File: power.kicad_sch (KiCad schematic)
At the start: 160 parts, among them Q10 SI7613DN-T1-GE3, Q14 BC817-25W, Q15 BC817-25W, Q2 BC817-25W, Q3 DZDH0401DW, Q4 DZDH0401DW, Q5 SI7613DN-T1-GE3, Q6 SI7613DN-T1-GE3, Q7 BC817-25W, Q8 BC817-25W, Q9 SI7613DN-T1-GE3, U1 LT8350RV#PBF, U10 LM3881MME_NOPB, U2 MP2386GG, U3 TPS65983BAZBHR, U9 LM1117MP-3.3_NOPB

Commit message: Run kmake loclib
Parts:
- C10, C13, C15, C17, C8: footprint antmicro-footprints:C_1206_3216Metric -> thunderbolt-adapter-footprints:C_1206_3216Metric; symbol antmicroCapacitorsmisc:C_22u_1206_35V -> thunderbolt-adapter:C_22u_1206_35V
- C11, C12, C127, C128, C7, C9: footprint antmicro-footprints:C_0805_2012Metric -> thunderbolt-adapter-footprints:C_0805_2012Metric; symbol antmicroCapacitorsmisc:C_10u_0805_35V -> thunderbolt-adapter:C_10u_0805_35V
- C119, C122, C38, C40, C43, C46, C50: footprint antmicro-footprints:C_0603_1608Metric -> thunderbolt-adapter-footprints:C_0603_1608Metric; symbol antmicroCapacitors0603:C_22u_16V_0603 -> thunderbolt-adapter:C_22u_16V_0603
- C129, C14, C24, C26, C28, C29, C32: footprint antmicro-footprints:C_0402_1005Metric -> thunderbolt-adapter-footprints:C_0402_1005Metric; symbol antmicroCapacitors0402:C_100n_0402 -> thunderbolt-adapter:C_100n_0402
- C130: footprint antmicro-footprints:C_0402_1005Metric -> thunderbolt-adapter-footprints:C_0402_1005Metric; symbol antmicroCapacitors0402:C_10n_0402 -> thunderbolt-adapter:C_10n_0402
- C16, C27, C31: footprint antmicro-footprints:C_0402_1005Metric -> thunderbolt-adapter-footprints:C_0402_1005Metric; symbol antmicroCapacitors0402:C_220n_0402 -> thunderbolt-adapter:C_220n_0402
- C18, C22, C25, C34: footprint antmicro-footprints:C_0402_1005Metric -> thunderbolt-adapter-footprints:C_0402_1005Metric; symbol antmicroCapacitors0402:C_1u_0402 -> thunderbolt-adapter:C_1u_0402
- C19: footprint antmicro-footprints:C_0402_1005Metric -> thunderbolt-adapter-footprints:C_0402_1005Metric; symbol antmicroCapacitors0402:C_22n_0402 -> thunderbolt-adapter:C_22n_0402
- C20, C21: footprint antmicro-footprints:C_0402_1005Metric -> thunderbolt-adapter-footprints:C_0402_1005Metric; symbol antmicroCapacitors0402:C_4u7_25V_0402 -> thunderbolt-adapter:C_4u7_25V_0402
- C23, C39: footprint antmicro-footprints:C_0402_1005Metric -> thunderbolt-adapter-footprints:C_0402_1005Metric; symbol antmicroCapacitors0402:C_10u_0402 -> thunderbolt-adapter:C_10u_0402
- C30: footprint antmicro-footprints:C_0402_1005Metric -> thunderbolt-adapter-footprints:C_0402_1005Metric; symbol antmicroCapacitors0402:C_4n7_0402 -> thunderbolt-adapter:C_4n7_0402
- C33: footprint antmicro-footprints:C_0402_1005Metric -> thunderbolt-adapter-footprints:C_0402_1005Metric; symbol antmicroCapacitors0402:C_33p_0402 -> thunderbolt-adapter:C_33p_0402
- C35, C36, C37: footprint antmicro-footprints:C_0402_1005Metric -> thunderbolt-adapter-footprints:C_0402_1005Metric; symbol antmicroCapacitors0402:C_2u2_0402 -> thunderbolt-adapter:C_2u2_0402
- C41, C44, C47: footprint antmicro-footprints:C_0603_1608Metric -> thunderbolt-adapter-footprints:C_0603_1608Metric; symbol antmicroCapacitors0603:C_22u_0603 -> thunderbolt-adapter:C_22u_0603
- C42, C48: footprint antmicro-footprints:C_0805_2012Metric -> thunderbolt-adapter-footprints:C_0805_2012Metric; symbol antmicroCapacitorsmisc:C_22u_25V_0805 -> thunderbolt-adapter:C_22u_25V_0805
- C45, C49: footprint antmicro-footprints:C_0402_1005Metric -> thunderbolt-adapter-footprints:C_0402_1005Metric; symbol antmicroCapacitors0402:C_220p_0402 -> thunderbolt-adapter:C_220p_0402
- D1: footprint antmicro-footprints:D_SOD-323F -> thunderbolt-adapter-footprints:D_SOD-323F; symbol antmicroDiodesZenerSingle:MM3Z3V3C -> thunderbolt-adapter:MM3Z3V3C
- D2, D3, D5: footprint antmicro-footprints:LED_0603_1608Metric_G -> thunderbolt-adapter-footprints:LED_0603_1608Metric_G; symbol antmicroLEDIndicationDiscrete:LED_G_0603_KP-1608CGCK -> thunderbolt-adapter:LED_G_0603_KP-1608CGCK
- FB1, FB2, FB3, FB5, FB6: footprint antmicro-footprints:FB_0805_2012Metric -> thunderbolt-adapter-footprints:FB_0805_2012Metric; symbol antmicroFerriteBeadsandChips:BLM21SN300SZ1D -> thunderbolt-adapter:BLM21SN300SZ1D
- L1: footprint antmicro-footprints:L_Coilcraft-XAL7070 -> thunderbolt-adapter-footprints:L_Coilcraft-XAL7070; symbol antmicroFixedInductors:L_6u8_12.8A_Coilcraft-XAL7070 -> thunderbolt-adapter:L_6u8_12.8A_Coilcraft-XAL7070
- L2: footprint antmicro-footprints:L_Coilcraft-XAL5030 -> thunderbolt-adapter-footprints:L_Coilcraft-XAL5030; symbol antmicroFixedInductors:L_2u2_9.7A_Coilcraft-XAL5030 -> thunderbolt-adapter:L_2u2_9.7A_Coilcraft-XAL5030
- Q10, Q5, Q6, Q9: footprint antmicro-footprints:Vishay_PowerPAK_1212-8_Single -> thunderbolt-adapter-footprints:Vishay_PowerPAK_1212-8_Single; symbol antmicroTransistorsFETsMOSFETsSingle:SI7613DN-T1-GE3 -> thunderbolt-adapter:SI7613DN-T1-GE3
- Q14, Q15, Q2, Q7, Q8: footprint antmicro-footprints:SOT-323 -> thunderbolt-adapter-footprints:SOT-323; symbol antmicroTransistorsBipolarSingle:BC817-25W -> thunderbolt-adapter:BC817-25W
- Q3, Q4: footprint antmicro-footprints:SOT-363 -> thunderbolt-adapter-footprints:SOT-363; symbol antmicroPMICORControllersIdealDiodes:DZDH0401DW -> thunderbolt-adapter:DZDH0401DW
- R10, R121, R122, R124, R125, R135, R137, R139, R140, R141, R22, R23, R24, R29, R30, R33, R34, R4, R9, R92, R95, R96: footprint antmicro-footprints:R_0402_1005Metric -> thunderbolt-adapter-footprints:R_0402_1005Metric; symbol antmicroResistors0402:R_100k_0402 -> thunderbolt-adapter:R_100k_0402
- R11, R16, R17, R19, R2, R20, R32, R39, R44, R6, R8, R91, R93, R94: footprint antmicro-footprints:R_0402_1005Metric -> thunderbolt-adapter-footprints:R_0402_1005Metric; symbol antmicroResistors0402:R_10k_0402 -> thunderbolt-adapter:R_10k_0402
- R116, R120, R134, R136, R142, R143, R144: footprint antmicro-footprints:R_0402_1005Metric -> thunderbolt-adapter-footprints:R_0402_1005Metric; symbol antmicroResistors0402:R_1k_0402 -> thunderbolt-adapter:R_1k_0402
- R12, R123, R13, R138, R18, R26, R27, R31: footprint antmicro-footprints:R_0402_1005Metric -> thunderbolt-adapter-footprints:R_0402_1005Metric; symbol antmicroResistors0402:R_0R_0402 -> thunderbolt-adapter:R_0R_0402
- R14, R15: footprint antmicro-footprints:R_0402_1005Metric -> thunderbolt-adapter-footprints:R_0402_1005Metric; symbol antmicroResistors0402:R_3k3_0402 -> thunderbolt-adapter:R_3k3_0402
- R21: footprint antmicro-footprints:R_0402_1005Metric -> thunderbolt-adapter-footprints:R_0402_1005Metric; symbol antmicroResistors0402:R_1M_0402 -> thunderbolt-adapter:R_1M_0402
- R25: footprint antmicro-footprints:R_0402_1005Metric -> thunderbolt-adapter-footprints:R_0402_1005Metric; symbol antmicroResistors0402:R_12k_0402 -> thunderbolt-adapter:R_12k_0402
- R28: footprint antmicro-footprints:R_0402_1005Metric -> thunderbolt-adapter-footprints:R_0402_1005Metric; symbol antmicroResistors0402:R_124k_0402 -> thunderbolt-adapter:R_124k_0402
- R3, R46, R5, R97: footprint antmicro-footprints:R_0402_1005Metric -> thunderbolt-adapter-footprints:R_0402_1005Metric; symbol antmicroResistors0402:R_2k2_0402 -> thunderbolt-adapter:R_2k2_0402
- R35: footprint antmicro-footprints:R_0402_1005Metric -> thunderbolt-adapter-footprints:R_0402_1005Metric; symbol antmicroResistors0402:R_15k_0.1%_0402 -> thunderbolt-adapter:R_15k_0.1%_0402
- R36: footprint antmicro-footprints:R_0402_1005Metric -> thunderbolt-adapter-footprints:R_0402_1005Metric; symbol antmicroResistors0402:R_40k2_0402 -> thunderbolt-adapter:R_40k2_0402
- R37: footprint antmicro-footprints:R_0402_1005Metric -> thunderbolt-adapter-footprints:R_0402_1005Metric; symbol antmicroResistors0402:R_8k87_0402 -> thunderbolt-adapter:R_8k87_0402
- R38, R40: footprint antmicro-footprints:R_0402_1005Metric -> thunderbolt-adapter-footprints:R_0402_1005Metric; symbol antmicroResistors0402:R_5k1_0402 -> thunderbolt-adapter:R_5k1_0402
- R41: footprint antmicro-footprints:R_0603_1608Metric -> thunderbolt-adapter-footprints:R_0603_1608Metric; symbol antmicroResistors0603:R_0R_0603 -> thunderbolt-adapter:R_0R_0603
- R42: footprint antmicro-footprints:R_0402_1005Metric -> thunderbolt-adapter-footprints:R_0402_1005Metric; symbol antmicroResistors0402:R_330R_0402 -> thunderbolt-adapter:R_330R_0402
- R43: footprint antmicro-footprints:R_0402_1005Metric -> thunderbolt-adapter-footprints:R_0402_1005Metric; symbol antmicroResistors0402:R_110k_0402 -> thunderbolt-adapter:R_110k_0402
- R45: footprint antmicro-footprints:R_1206_3216Metric -> thunderbolt-adapter-footprints:R_1206_3216Metric; symbol antmicroResistorsmisc:R_0R02_1206 -> thunderbolt-adapter:R_0R02_1206
- R7: footprint antmicro-footprints:R_0402_1005Metric -> thunderbolt-adapter-footprints:R_0402_1005Metric; symbol antmicroResistors0402:R_24k_0402 -> thunderbolt-adapter:R_24k_0402
- R98, R99: footprint antmicro-footprints:R_0603_1608Metric -> thunderbolt-adapter-footprints:R_0603_1608Metric; symbol antmicroResistors0603:R_0R_22.4A_0603 -> thunderbolt-adapter:R_0R_22.4A_0603
- TP1, TP12, TP2, TP3, TP5, TP7, TP8: footprint antmicro-footprints:Testpoint_smd_1mm -> thunderbolt-adapter-footprints:Testpoint_smd_1mm; symbol antmicroTestPoints:TP_1mm_SMD -> thunderbolt-adapter:TP_1mm_SMD
- TP10, TP11: footprint antmicro-footprints:NetTie-2_SMD_Pad0.127mm -> thunderbolt-adapter-footprints:NetTie-2_SMD_Pad0.127mm; symbol antmicroShuntsJumpers:Net-Tie_2 -> thunderbolt-adapter:Net-Tie_2
- TP4, TP6: footprint antmicro-footprints:TP_SMD_0.75mm -> thunderbolt-adapter-footprints:TP_SMD_0.75mm; symbol antmicroTestPoints:TP_0.75mm_SMD -> thunderbolt-adapter:TP_0.75mm_SMD
- U1: footprint antmicro-footprints:QFN-32-4EP_4x6mm_P0.5mm -> thunderbolt-adapter-footprints:QFN-32-4EP_4x6mm_P0.5mm; symbol antmicroDCDCConverters:LT8350RV#PBF -> thunderbolt-adapter:LT8350RV#PBF
- U10: footprint antmicro-footprints:VSSOP-8_3x3mm_P0.65mm -> thunderbolt-adapter-footprints:VSSOP-8_3x3mm_P0.65mm; symbol antmicroPMICPowerSequencers:LM3881MME_NOPB -> thunderbolt-adapter:LM3881MME_NOPB
- U2: footprint antmicro-footprints:QFN-11_2x2mm_P0.5mm -> thunderbolt-adapter-footprints:QFN-11_2x2mm_P0.5mm; symbol antmicroDCDCConverters:MP2386GG -> thunderbolt-adapter:MP2386GG
- U3: footprint antmicro-footprints:IC_TPS65983BAZBHR -> thunderbolt-adapter-footprints:IC_TPS65983BAZBHR; symbol antmicroInterfaceControllers:TPS65983BAZBHR -> thunderbolt-adapter:TPS65983BAZBHR
- U9: footprint antmicro-footprints:SOT-223 -> thunderbolt-adapter-footprints:SOT-223; symbol antmicroPMICVoltageRegulatorsLinear:LM1117MP-3.3_NOPB -> thunderbolt-adapter:LM1117MP-3.3_NOPB

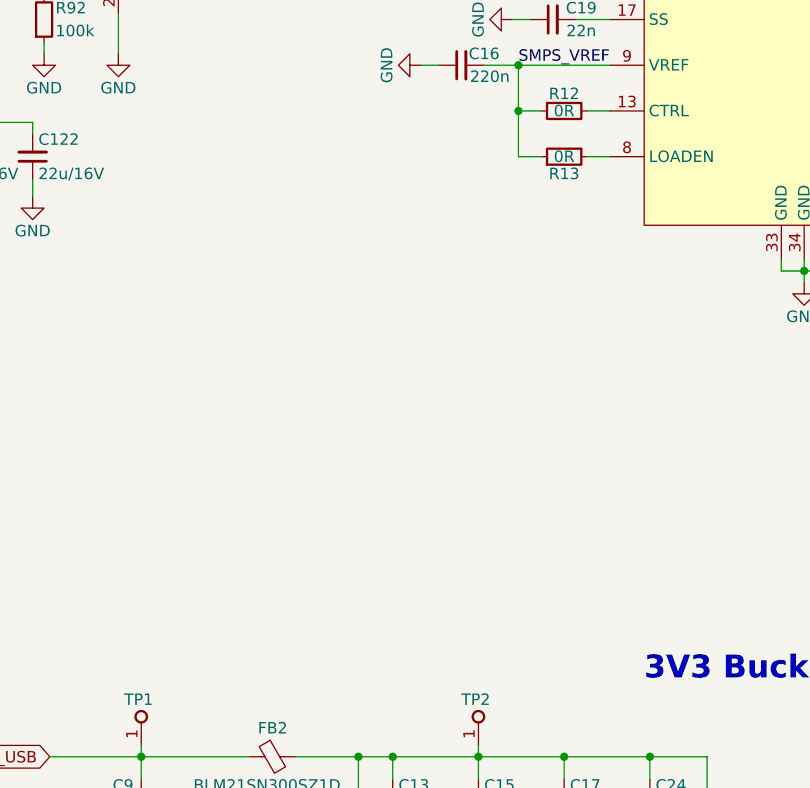
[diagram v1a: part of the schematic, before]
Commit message: Rename project to thunderbolt-gpu-adapter
Fix Amphenol 10146070-113Y0LF footprint
Add missing 3D models, update selected footprints
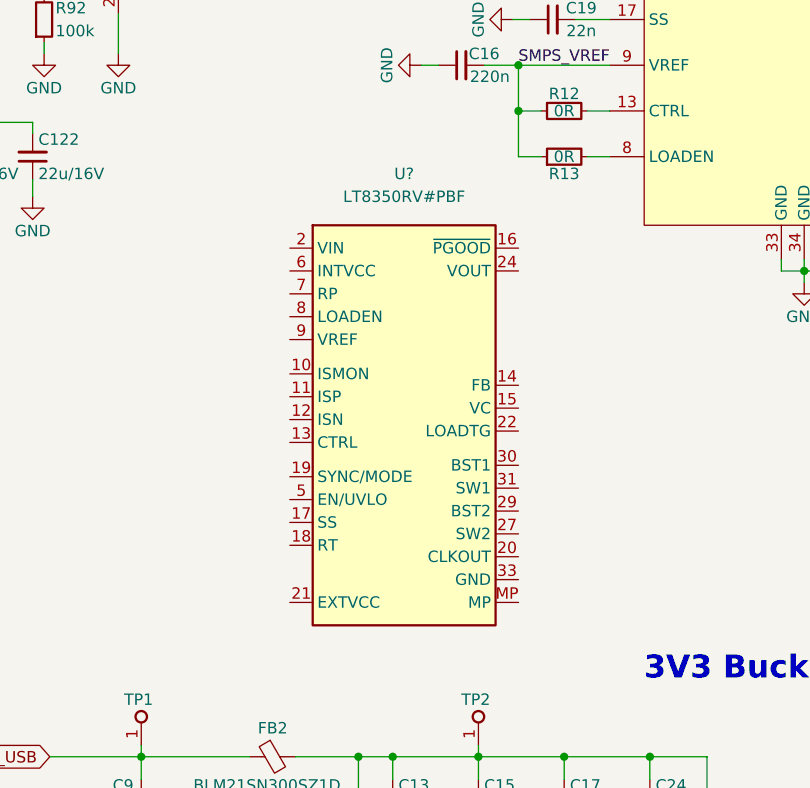
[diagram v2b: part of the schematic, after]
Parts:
- added U?: LT8350RV, thunderbolt-gpu-adapter-footprints:QFN-32-4EP_4x6mm_P0.5mm, symbol thunderbolt-gpu-adapter:LT8350RV
- C10, C13, C15, C17, C8: footprint thunderbolt-adapter-footprints:C_1206_3216Metric -> thunderbolt-gpu-adapter-footprints:C_1206_3216Metric; symbol thunderbolt-adapter:C_22u_1206_35V -> thunderbolt-gpu-adapter:C_22u_1206_35V
- C11, C12, C127, C128, C7, C9: footprint thunderbolt-adapter-footprints:C_0805_2012Metric -> thunderbolt-gpu-adapter-footprints:C_0805_2012Metric; symbol thunderbolt-adapter:C_10u_0805_35V -> thunderbolt-gpu-adapter:C_10u_0805_35V
- C119, C122, C38, C40, C43, C46, C50: footprint thunderbolt-adapter-footprints:C_0603_1608Metric -> thunderbolt-gpu-adapter-footprints:C_0603_1608Metric; symbol thunderbolt-adapter:C_22u_16V_0603 -> thunderbolt-gpu-adapter:C_22u_16V_0603
- C129, C14, C24, C26, C28, C29, C32: footprint thunderbolt-adapter-footprints:C_0402_1005Metric -> thunderbolt-gpu-adapter-footprints:C_0402_1005Metric; symbol thunderbolt-adapter:C_100n_0402 -> thunderbolt-gpu-adapter:C_100n_0402
- C130: footprint thunderbolt-adapter-footprints:C_0402_1005Metric -> thunderbolt-gpu-adapter-footprints:C_0402_1005Metric; symbol thunderbolt-adapter:C_10n_0402 -> thunderbolt-gpu-adapter:C_10n_0402
- C16, C27, C31: footprint thunderbolt-adapter-footprints:C_0402_1005Metric -> thunderbolt-gpu-adapter-footprints:C_0402_1005Metric; symbol thunderbolt-adapter:C_220n_0402 -> thunderbolt-gpu-adapter:C_220n_0402
- C18, C22, C25, C34: footprint thunderbolt-adapter-footprints:C_0402_1005Metric -> thunderbolt-gpu-adapter-footprints:C_0402_1005Metric; symbol thunderbolt-adapter:C_1u_0402 -> thunderbolt-gpu-adapter:C_1u_0402
- C19: footprint thunderbolt-adapter-footprints:C_0402_1005Metric -> thunderbolt-gpu-adapter-footprints:C_0402_1005Metric; symbol thunderbolt-adapter:C_22n_0402 -> thunderbolt-gpu-adapter:C_22n_0402
- C20, C21: footprint thunderbolt-adapter-footprints:C_0402_1005Metric -> thunderbolt-gpu-adapter-footprints:C_0402_1005Metric; symbol thunderbolt-adapter:C_4u7_25V_0402 -> thunderbolt-gpu-adapter:C_4u7_25V_0402
- C23, C39: footprint thunderbolt-adapter-footprints:C_0402_1005Metric -> thunderbolt-gpu-adapter-footprints:C_0402_1005Metric; symbol thunderbolt-adapter:C_10u_0402 -> thunderbolt-gpu-adapter:C_10u_0402
- C30: footprint thunderbolt-adapter-footprints:C_0402_1005Metric -> thunderbolt-gpu-adapter-footprints:C_0402_1005Metric; symbol thunderbolt-adapter:C_4n7_0402 -> thunderbolt-gpu-adapter:C_4n7_0402
- C33: footprint thunderbolt-adapter-footprints:C_0402_1005Metric -> thunderbolt-gpu-adapter-footprints:C_0402_1005Metric; symbol thunderbolt-adapter:C_33p_0402 -> thunderbolt-gpu-adapter:C_33p_0402
- C35, C36, C37: footprint thunderbolt-adapter-footprints:C_0402_1005Metric -> thunderbolt-gpu-adapter-footprints:C_0402_1005Metric; symbol thunderbolt-adapter:C_2u2_0402 -> thunderbolt-gpu-adapter:C_2u2_0402
- C41, C44, C47: footprint thunderbolt-adapter-footprints:C_0603_1608Metric -> thunderbolt-gpu-adapter-footprints:C_0603_1608Metric; symbol thunderbolt-adapter:C_22u_0603 -> thunderbolt-gpu-adapter:C_22u_0603
- C42, C48: footprint thunderbolt-adapter-footprints:C_0805_2012Metric -> thunderbolt-gpu-adapter-footprints:C_0805_2012Metric; symbol thunderbolt-adapter:C_22u_25V_0805 -> thunderbolt-gpu-adapter:C_22u_25V_0805
- C45, C49: footprint thunderbolt-adapter-footprints:C_0402_1005Metric -> thunderbolt-gpu-adapter-footprints:C_0402_1005Metric; symbol thunderbolt-adapter:C_220p_0402 -> thunderbolt-gpu-adapter:C_220p_0402
- D1: footprint thunderbolt-adapter-footprints:D_SOD-323F -> thunderbolt-gpu-adapter-footprints:D_SOD-323F; symbol thunderbolt-adapter:MM3Z3V3C -> thunderbolt-gpu-adapter:MM3Z3V3C
- D2, D3, D5: footprint thunderbolt-adapter-footprints:LED_0603_1608Metric_G -> thunderbolt-gpu-adapter-footprints:LED_0603_1608Metric_G; symbol thunderbolt-adapter:LED_G_0603_KP-1608CGCK -> thunderbolt-gpu-adapter:LED_G_0603_KP-1608CGCK
- FB1, FB2, FB3, FB5, FB6: footprint thunderbolt-adapter-footprints:FB_0805_2012Metric -> thunderbolt-gpu-adapter-footprints:FB_0805_2012Metric; symbol thunderbolt-adapter:BLM21SN300SZ1D -> thunderbolt-gpu-adapter:BLM21SN300SZ1D
- L1: footprint thunderbolt-adapter-footprints:L_Coilcraft-XAL7070 -> thunderbolt-gpu-adapter-footprints:L_Coilcraft-XAL7070; symbol thunderbolt-adapter:L_6u8_12.8A_Coilcraft-XAL7070 -> thunderbolt-gpu-adapter:L_6u8_12.8A_Coilcraft-XAL7070
- L2: footprint thunderbolt-adapter-footprints:L_Coilcraft-XAL5030 -> thunderbolt-gpu-adapter-footprints:L_Coilcraft-XAL5030; symbol thunderbolt-adapter:L_2u2_9.7A_Coilcraft-XAL5030 -> thunderbolt-gpu-adapter:L_2u2_9.7A_Coilcraft-XAL5030
- Q10, Q5, Q6, Q9: footprint thunderbolt-adapter-footprints:Vishay_PowerPAK_1212-8_Single -> thunderbolt-gpu-adapter-footprints:Vishay_PowerPAK_1212-8_Single; symbol thunderbolt-adapter:SI7613DN-T1-GE3 -> thunderbolt-gpu-adapter:SI7613DN-T1-GE3
- Q14, Q15, Q2, Q7, Q8: footprint thunderbolt-adapter-footprints:SOT-323 -> thunderbolt-gpu-adapter-footprints:SOT-323; symbol thunderbolt-adapter:BC817-25W -> thunderbolt-gpu-adapter:BC817-25W
- Q3, Q4: footprint thunderbolt-adapter-footprints:SOT-363 -> thunderbolt-gpu-adapter-footprints:SOT-363; symbol thunderbolt-adapter:DZDH0401DW -> thunderbolt-gpu-adapter:DZDH0401DW
- R10, R121, R122, R124, R125, R135, R137, R139, R140, R141, R22, R23, R24, R29, R30, R33, R34, R4, R9, R92, R95, R96: footprint thunderbolt-adapter-footprints:R_0402_1005Metric -> thunderbolt-gpu-adapter-footprints:R_0402_1005Metric; symbol thunderbolt-adapter:R_100k_0402 -> thunderbolt-gpu-adapter:R_100k_0402
- R11, R16, R17, R19, R2, R20, R32, R39, R44, R6, R8, R91, R93, R94: footprint thunderbolt-adapter-footprints:R_0402_1005Metric -> thunderbolt-gpu-adapter-footprints:R_0402_1005Metric; symbol thunderbolt-adapter:R_10k_0402 -> thunderbolt-gpu-adapter:R_10k_0402
- R116, R120, R134, R136, R142, R143, R144: footprint thunderbolt-adapter-footprints:R_0402_1005Metric -> thunderbolt-gpu-adapter-footprints:R_0402_1005Metric; symbol thunderbolt-adapter:R_1k_0402 -> thunderbolt-gpu-adapter:R_1k_0402
- R12, R123, R13, R138, R18, R26, R27, R31: footprint thunderbolt-adapter-footprints:R_0402_1005Metric -> thunderbolt-gpu-adapter-footprints:R_0402_1005Metric; symbol thunderbolt-adapter:R_0R_0402 -> thunderbolt-gpu-adapter:R_0R_0402
- R14, R15: footprint thunderbolt-adapter-footprints:R_0402_1005Metric -> thunderbolt-gpu-adapter-footprints:R_0402_1005Metric; symbol thunderbolt-adapter:R_3k3_0402 -> thunderbolt-gpu-adapter:R_3k3_0402
- R21: footprint thunderbolt-adapter-footprints:R_0402_1005Metric -> thunderbolt-gpu-adapter-footprints:R_0402_1005Metric; symbol thunderbolt-adapter:R_1M_0402 -> thunderbolt-gpu-adapter:R_1M_0402
- R25: footprint thunderbolt-adapter-footprints:R_0402_1005Metric -> thunderbolt-gpu-adapter-footprints:R_0402_1005Metric; symbol thunderbolt-adapter:R_12k_0402 -> thunderbolt-gpu-adapter:R_12k_0402
- R28: footprint thunderbolt-adapter-footprints:R_0402_1005Metric -> thunderbolt-gpu-adapter-footprints:R_0402_1005Metric; symbol thunderbolt-adapter:R_124k_0402 -> thunderbolt-gpu-adapter:R_124k_0402
- R3, R46, R5, R97: footprint thunderbolt-adapter-footprints:R_0402_1005Metric -> thunderbolt-gpu-adapter-footprints:R_0402_1005Metric; symbol thunderbolt-adapter:R_2k2_0402 -> thunderbolt-gpu-adapter:R_2k2_0402
- R35: footprint thunderbolt-adapter-footprints:R_0402_1005Metric -> thunderbolt-gpu-adapter-footprints:R_0402_1005Metric; symbol thunderbolt-adapter:R_15k_0.1%_0402 -> thunderbolt-gpu-adapter:R_15k_0.1%_0402
- R36: footprint thunderbolt-adapter-footprints:R_0402_1005Metric -> thunderbolt-gpu-adapter-footprints:R_0402_1005Metric; symbol thunderbolt-adapter:R_40k2_0402 -> thunderbolt-gpu-adapter:R_40k2_0402
- R37: footprint thunderbolt-adapter-footprints:R_0402_1005Metric -> thunderbolt-gpu-adapter-footprints:R_0402_1005Metric; symbol thunderbolt-adapter:R_8k87_0402 -> thunderbolt-gpu-adapter:R_8k87_0402
- R38, R40: footprint thunderbolt-adapter-footprints:R_0402_1005Metric -> thunderbolt-gpu-adapter-footprints:R_0402_1005Metric; symbol thunderbolt-adapter:R_5k1_0402 -> thunderbolt-gpu-adapter:R_5k1_0402
- R41: footprint thunderbolt-adapter-footprints:R_0603_1608Metric -> thunderbolt-gpu-adapter-footprints:R_0603_1608Metric; symbol thunderbolt-adapter:R_0R_0603 -> thunderbolt-gpu-adapter:R_0R_0603
- R42: footprint thunderbolt-adapter-footprints:R_0402_1005Metric -> thunderbolt-gpu-adapter-footprints:R_0402_1005Metric; symbol thunderbolt-adapter:R_330R_0402 -> thunderbolt-gpu-adapter:R_330R_0402
- R43: footprint thunderbolt-adapter-footprints:R_0402_1005Metric -> thunderbolt-gpu-adapter-footprints:R_0402_1005Metric; symbol thunderbolt-adapter:R_110k_0402 -> thunderbolt-gpu-adapter:R_110k_0402
- R45: footprint thunderbolt-adapter-footprints:R_1206_3216Metric -> thunderbolt-gpu-adapter-footprints:R_1206_3216Metric; symbol thunderbolt-adapter:R_0R02_1206 -> thunderbolt-gpu-adapter:R_0R02_1206
- R7: footprint thunderbolt-adapter-footprints:R_0402_1005Metric -> thunderbolt-gpu-adapter-footprints:R_0402_1005Metric; symbol thunderbolt-adapter:R_24k_0402 -> thunderbolt-gpu-adapter:R_24k_0402
- R98, R99: footprint thunderbolt-adapter-footprints:R_0603_1608Metric -> thunderbolt-gpu-adapter-footprints:R_0603_1608Metric; symbol thunderbolt-adapter:R_0R_22.4A_0603 -> thunderbolt-gpu-adapter:R_0R_22.4A_0603
- TP1, TP12, TP2, TP3, TP5, TP7, TP8: footprint thunderbolt-adapter-footprints:Testpoint_smd_1mm -> thunderbolt-gpu-adapter-footprints:Testpoint_smd_1mm; symbol thunderbolt-adapter:TP_1mm_SMD -> thunderbolt-gpu-adapter:TP_1mm_SMD
- TP10, TP11: footprint thunderbolt-adapter-footprints:NetTie-2_SMD_Pad0.127mm -> thunderbolt-gpu-adapter-footprints:NetTie-2_SMD_Pad0.127mm; symbol thunderbolt-adapter:Net-Tie_2 -> thunderbolt-gpu-adapter:Net-Tie_2
- TP4, TP6: footprint thunderbolt-adapter-footprints:TP_SMD_0.75mm -> thunderbolt-gpu-adapter-footprints:TP_SMD_0.75mm; symbol thunderbolt-adapter:TP_0.75mm_SMD -> thunderbolt-gpu-adapter:TP_0.75mm_SMD
- U1: footprint thunderbolt-adapter-footprints:QFN-32-4EP_4x6mm_P0.5mm -> thunderbolt-gpu-adapter-footprints:QFN-32-4EP_4x6mm_P0.5mm; symbol thunderbolt-adapter:LT8350RV#PBF -> thunderbolt-gpu-adapter:LT8350RV#PBF
- U10: footprint thunderbolt-adapter-footprints:VSSOP-8_3x3mm_P0.65mm -> thunderbolt-gpu-adapter-footprints:VSSOP-8_3x3mm_P0.65mm; symbol thunderbolt-adapter:LM3881MME_NOPB -> thunderbolt-gpu-adapter:LM3881MME_NOPB
- U2: footprint thunderbolt-adapter-footprints:QFN-11_2x2mm_P0.5mm -> thunderbolt-gpu-adapter-footprints:QFN-11_2x2mm_P0.5mm; symbol thunderbolt-adapter:MP2386GG -> thunderbolt-gpu-adapter:MP2386GG
- U3: footprint thunderbolt-adapter-footprints:IC_TPS65983BAZBHR -> thunderbolt-gpu-adapter-footprints:IC_TPS65983BAZBHR; symbol thunderbolt-adapter:TPS65983BAZBHR -> thunderbolt-gpu-adapter:TPS65983BAZBHR
- U9: footprint thunderbolt-adapter-footprints:SOT-223 -> thunderbolt-gpu-adapter-footprints:SOT-223; symbol thunderbolt-adapter:LM1117MP-3.3_NOPB -> thunderbolt-gpu-adapter:LM1117MP-3.3_NOPB
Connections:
- new net: U?.2 (VIN), U?.3 (VIN)
- new net: U?.24 (VOUT), U?.25 (VOUT)
- new net: U?.27 (SW2), U?.28 (SW2)
- new net: U?.31 (SW1), U?.32 (SW1)
- new net: U?.33 (GND), U?.34 (GND), U?.35 (GND), U?.36 (GND)
